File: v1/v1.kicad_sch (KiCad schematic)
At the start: 45 parts, among them CON1 SNES-CONN, M1 LY68L6400SLIT, U1 SN74LV165APWR, U2 SN74LV165APWR, U3 SN74LV165APWR, U4 SN74LVC8T245PWR, U5 PIC12F629-I/SN, U6 AMS1117-3.3, U7 SN74LVC8T245PWR, U8 Pair of 20-pin 1.27mm pitch v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

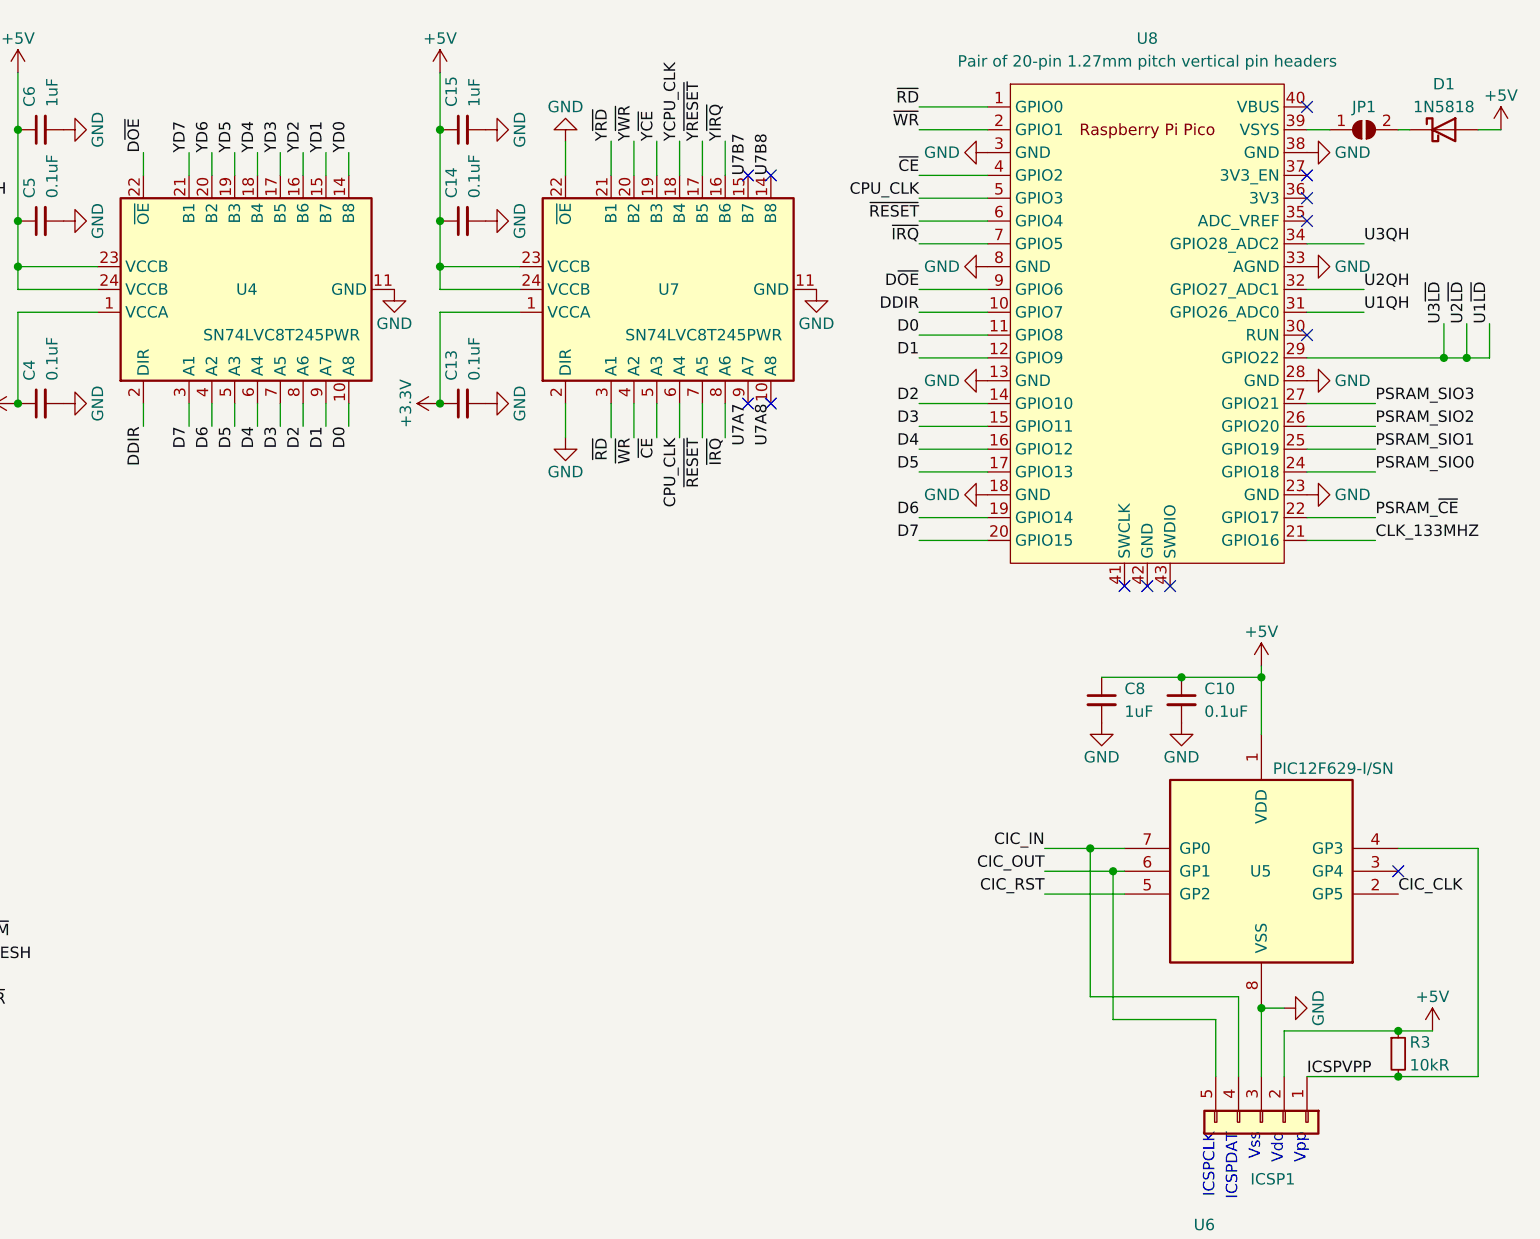
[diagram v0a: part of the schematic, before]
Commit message: v1: replace Pico component with pair of pin headers
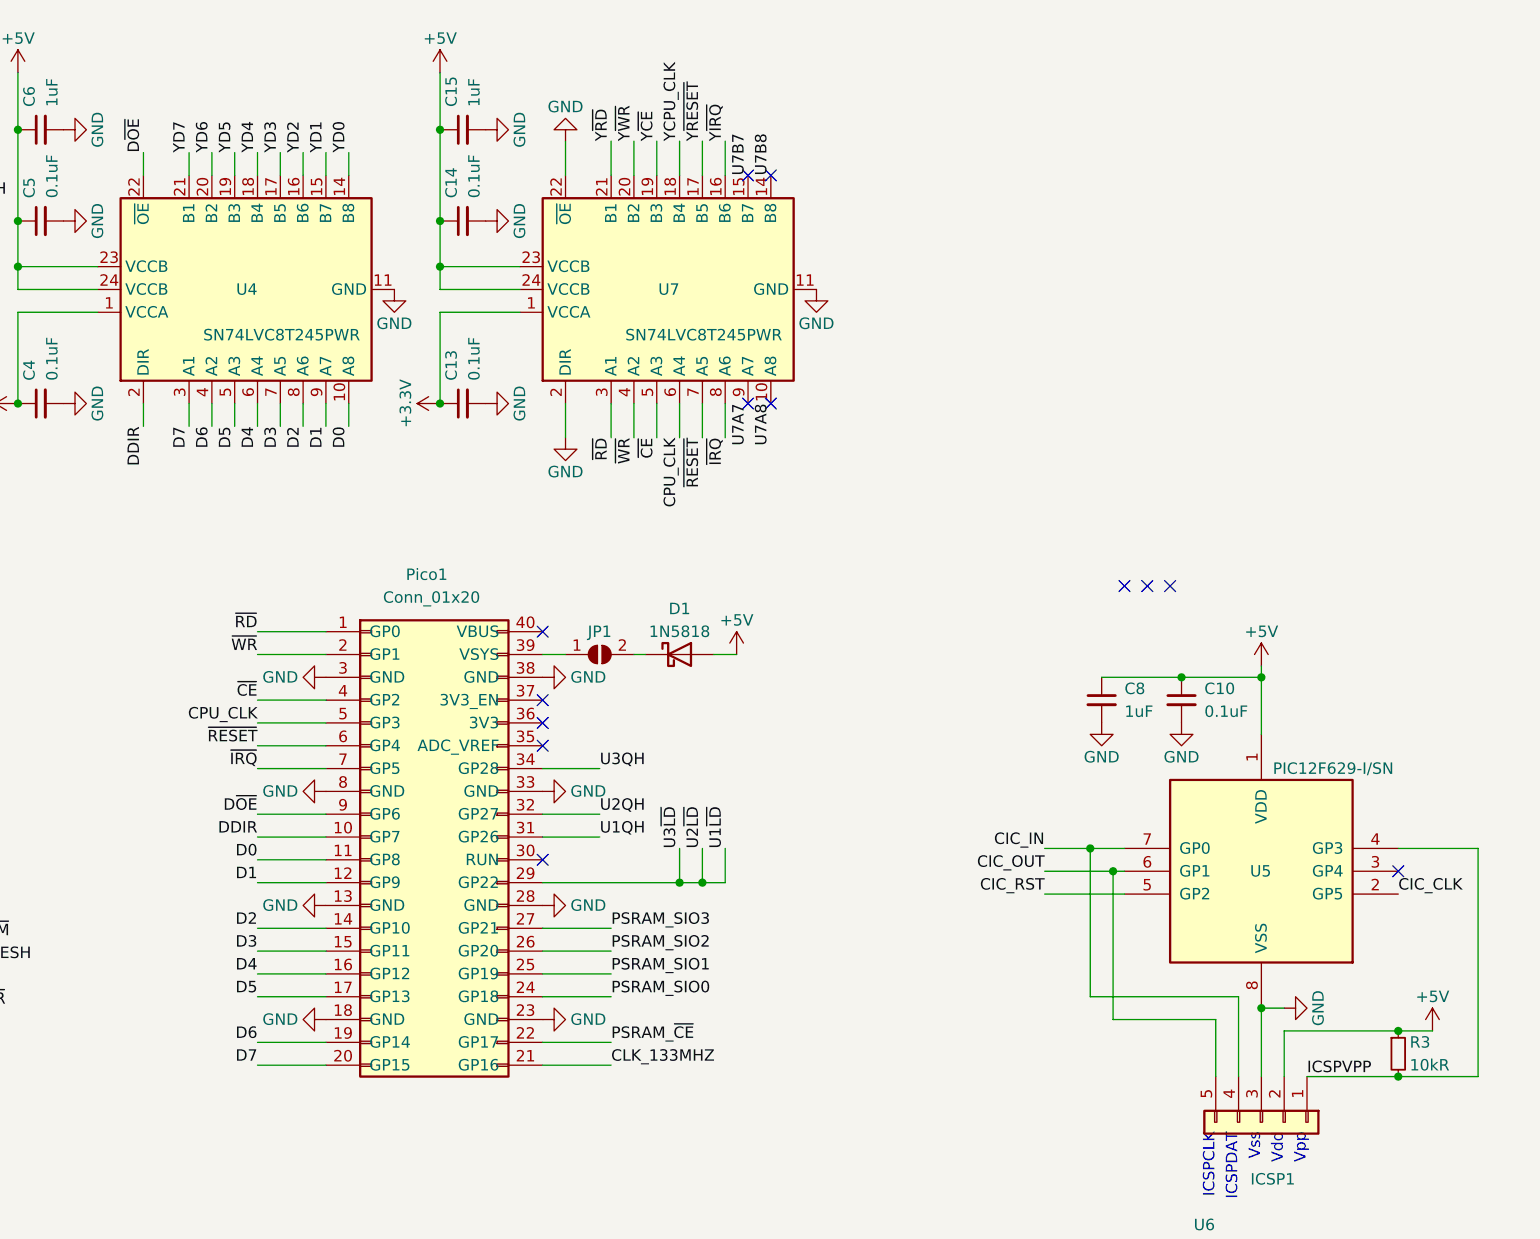
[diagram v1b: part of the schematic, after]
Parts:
- removed U8: Pair of 20-pin 1.27mm pitch vertical pin headers, RP-Pico:RPi_Pico_SMD_TH, symbol MCU_RaspberryPi_and_Boards:Pico
- added Pico1: Conn_01x20, Connector_PinHeader_2.54mm:PinHeader_1x20_P2.54mm_Vertical, symbol Connector_Generic:Conn_01x20
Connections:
- net CLK_133MHZ: now also Pico1.21 (GP16)
- net CPU_CLK: now also Pico1.5 (GP3)
- net D0: now also Pico1.11 (GP8)
- net D1: now also Pico1.12 (GP9)
- net D2: now also Pico1.14 (GP10)
- net D3: now also Pico1.15 (GP11)
- net D4: now also Pico1.16 (GP12)
- net D5: now also Pico1.17 (GP13)
- net D6: now also Pico1.19 (GP14)
- net D7: now also Pico1.20 (GP15)
- net DDIR: now also Pico1.10 (GP7)
- net D~{OE}: now also Pico1.9 (GP6)
- net GND: now also Pico1.13 (GND), Pico1.18 (GND), Pico1.23 (GND), Pico1.28 (GND), Pico1.3 (GND), Pico1.33 (GND), Pico1.38 (GND), Pico1.8 (GND)
- net PSRAM_SIO0: now also Pico1.24 (GP18)
- net PSRAM_SIO1: now also Pico1.25 (GP19)
- net PSRAM_SIO2: now also Pico1.26 (GP20)
- net PSRAM_SIO3: now also Pico1.27 (GP21)
- net PSRAM_~{CE}: now also Pico1.22 (GP17)
- net U1QH: now also Pico1.31 (GP26)
- net U1~{LD}: now also Pico1.29 (GP22)
- net U2QH: now also Pico1.32 (GP27)
- net U3QH: now also Pico1.34 (GP28)
- net ~{CE}: now also Pico1.4 (GP2)
- net ~{IRQ}: now also Pico1.7 (GP5)
- net ~{RD}: now also Pico1.1 (GP0)
- net ~{RESET}: now also Pico1.6 (GP4)
- net ~{WR}: now also Pico1.2 (GP1)
- net at JP1.1 (A): now also Pico1.39 (VSYS)

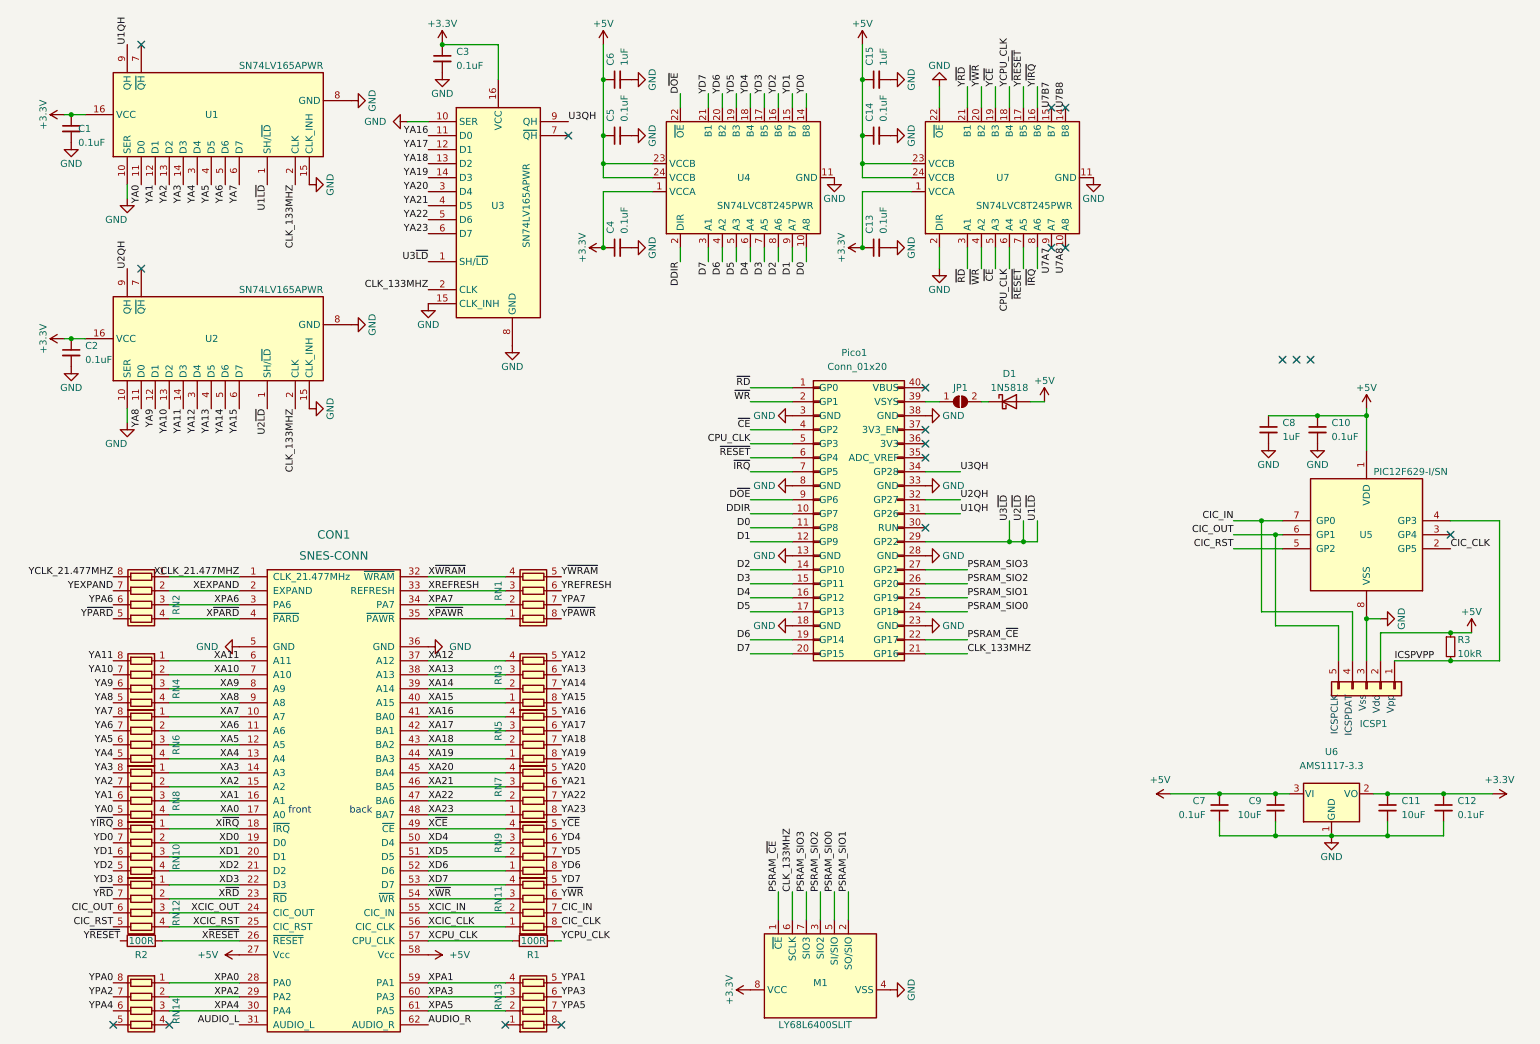
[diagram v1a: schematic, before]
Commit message: v1: redo shift regs; redo gpio pin assignments; add jumpers for LDO vs Pico 3V3 power supply; use TXS0101 for /RESET
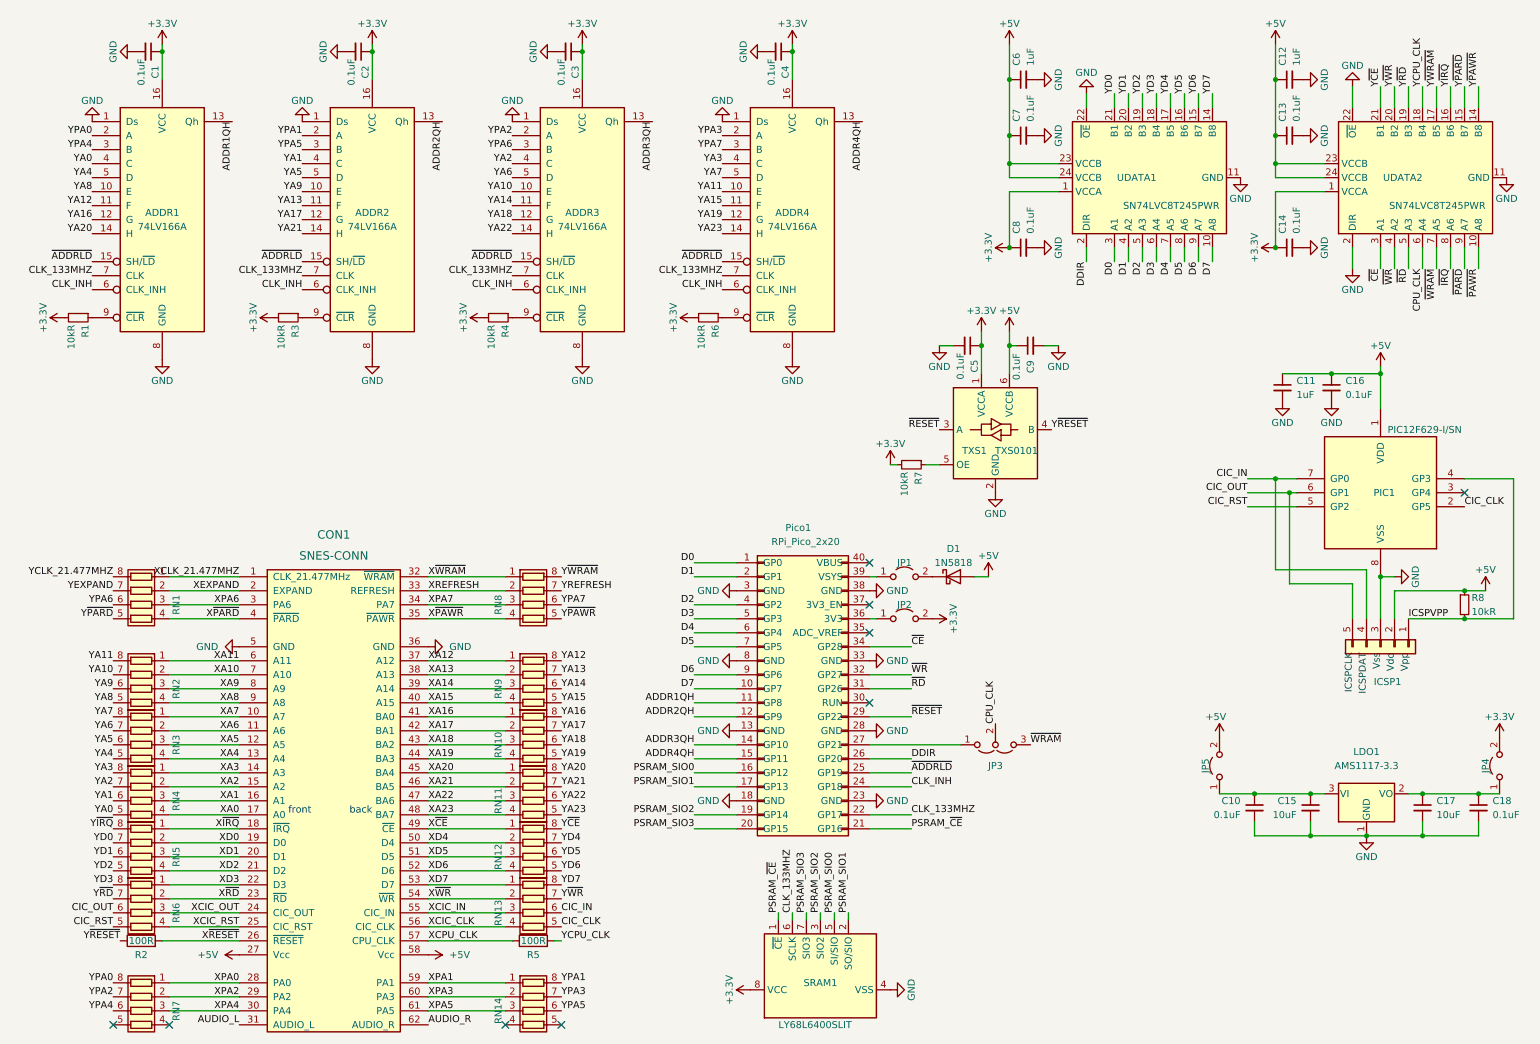
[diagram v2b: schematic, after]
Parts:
- removed RN3, RN5, RN7: 100R, Resistor_SMD:R_Array_Concave_4x0603, symbol Device:R_Pack04
- removed U1, U2, U3: SN74LV165APWR, Package_SO:TSSOP-16_4.4x5mm_P0.65mm, symbol 74xx:74HC165
- added ADDR1, ADDR2, ADDR3, ADDR4: 74LV166A, Package_SO:SOIC-16_3.9x9.9mm_P1.27mm, symbol 74xx:74LV166A
- added C4, C5, C9: 0.1uF, Capacitor_SMD:C_1206_3216Metric_Pad1.33x1.80mm_HandSolder, symbol Device:C_Small
- added JP2: PICO_3V3_EN, Connector_PinHeader_2.54mm:PinHeader_1x02_P2.54mm_Vertical, symbol Jumper:Jumper_2_Open
- added JP3: CLK_OR_WRAM, Connector_PinHeader_2.54mm:PinHeader_1x03_P2.54mm_Vertical, symbol Jumper:Jumper_3_Open
- added JP4: SNES_3V3_EN, Connector_PinHeader_2.54mm:PinHeader_1x02_P2.54mm_Vertical, symbol Jumper:Jumper_2_Open
- added JP5: LDO_EN, Connector_PinHeader_2.54mm:PinHeader_1x02_P2.54mm_Vertical, symbol Jumper:Jumper_2_Open
- added R1, R3, R4, R6, R7: 10kR, Resistor_SMD:R_1206_3216Metric_Pad1.30x1.75mm_HandSolder, symbol Device:R_Small
- added RN10, RN12, RN14: 100R, Resistor_SMD:R_Array_Concave_4x0603, symbol Device:R_Pack04
- added TXS1: TXS0101, Package_TO_SOT_SMD:SOT-23-6_Handsoldering, symbol Logic_LevelTranslator:TXS0101
- CON1: footprint sd2snes:SNESCART_EXT2_SMTUSB -> SNES:SNESCART_EXT2
- ICSP1: value Conn_01x05 -> PIC12_ICSP
- JP1: value SolderJumper_2_Open -> SNES 5V -> Pico; footprint Jumper:SolderJumper-2_P1.3mm_Open_RoundedPad1.0x1.5mm -> Connector_PinHeader_2.54mm:PinHeader_1x02_P2.54mm_Vertical; symbol Jumper:SolderJumper_2_Open -> Jumper:Jumper_2_Open
- Pico1: value Conn_01x20 -> RPi_Pico_2x20; footprint Connector_PinHeader_2.54mm:PinHeader_1x20_P2.54mm_Vertical -> RPi_Pico:RPi_Pico_2x20; symbol Connector_Generic:Conn_01x20 -> RPi_Pico:RPi_Pico
- renumbered C7 to C10, C8 to C11, C15 to C12, C14 to C13, C13 to C14, C9 to C15, C10 to C16, C11 to C17, C12 to C18, C5 to C7, C4 to C8, U6 to LDO1, U5 to PIC1, R1 to R5, R3 to R8, RN2 to RN1, RN4 to RN2, RN6 to RN3, RN8 to RN4, RN10 to RN5, RN12 to RN6, RN14 to RN7, RN1 to RN8, M1 to SRAM1, U4 to UDATA1, U7 to UDATA2
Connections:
- net U1QH is gone; now on net ~{RD}: Pico1.31 (GP26)
- net U1~{LD} is gone; now on net ~{RESET}: Pico1.29 (GP22)
- net U2QH is gone; now on net ~{WR}: Pico1.32 (GP27)
- net U3QH is gone; now on net ~{CE}: Pico1.34 (GP28)
- net U7B7 is gone; now on net Y~{PARD}: UDATA2.15 (B7)
- net U7B8 is gone; now on net Y~{PAWR}: UDATA2.14 (B8)
- net +3.3V: now also ADDR1.16 (VCC), ADDR2.16 (VCC), ADDR3.16 (VCC), ADDR4.16 (VCC), C4.1, C5.1, JP2.2 (B), JP4.2 (B), R1.2, R3.2, R4.2, R6.2, R7.2, TXS1.1 (VCCA); no longer C17.1, C18.1, LDO1.2 (VO)
- net +5V: now also C9.1, JP5.2 (B), TXS1.6 (VCCB); no longer C10.1, C15.1, LDO1.3 (VI)
- net CIC_CLK: now also RN13.5 (R4.2); no longer RN11.8 (R1.2)
- net CIC_IN: now also RN13.6 (R3.2); no longer RN11.7 (R2.2)
- net CLK_133MHZ: now also Pico1.22 (GP17), ADDR1.7 (CLK), ADDR2.7 (CLK), ADDR3.7 (CLK), ADDR4.7 (CLK); no longer Pico1.21 (GP16)
- net CPU_CLK: now also JP3.2 (C); no longer Pico1.5 (GP3)
- net D0: now also Pico1.1 (GP0), UDATA1.3 (A1); no longer Pico1.11 (GP8), UDATA1.10 (A8)
- net D1: now also Pico1.2 (GP1), UDATA1.4 (A2); no longer Pico1.12 (GP9), UDATA1.9 (A7)
- net D2: now also Pico1.4 (GP2), UDATA1.5 (A3); no longer Pico1.14 (GP10), UDATA1.8 (A6)
- net D3: now also Pico1.5 (GP3), UDATA1.6 (A4); no longer Pico1.15 (GP11), UDATA1.7 (A5)
- net D4: now also Pico1.6 (GP4), UDATA1.7 (A5); no longer Pico1.16 (GP12), UDATA1.6 (A4)
- net D5: now also Pico1.7 (GP5), UDATA1.8 (A6); no longer Pico1.17 (GP13), UDATA1.5 (A3)
- net D6: now also Pico1.9 (GP6), UDATA1.9 (A7); no longer Pico1.19 (GP14), UDATA1.4 (A2)
- net D7: now also Pico1.10 (GP7), UDATA1.10 (A8); no longer Pico1.20 (GP15), UDATA1.3 (A1)
- net DDIR: now also Pico1.26 (GP20); no longer Pico1.10 (GP7)
- net GND: now also UDATA1.22 (~{OE}), ADDR1.1 (Ds), ADDR1.8 (GND), ADDR2.1 (Ds), ADDR2.8 (GND), ADDR3.1 (Ds), ADDR3.8 (GND), ADDR4.1 (Ds), ADDR4.8 (GND), C4.2, C5.2, C9.2, TXS1.2 (GND)
- net PSRAM_SIO0: now also Pico1.16 (GP12); no longer Pico1.24 (GP18)
- net PSRAM_SIO1: now also Pico1.17 (GP13); no longer Pico1.25 (GP19)
- net PSRAM_SIO2: now also Pico1.19 (GP14); no longer Pico1.26 (GP20)
- net PSRAM_SIO3: now also Pico1.20 (GP15); no longer Pico1.27 (GP21)
- net PSRAM_~{CE}: now also Pico1.21 (GP16); no longer Pico1.22 (GP17)
- net XA12: now also RN9.1 (R1.1)
- net XA13: now also RN9.2 (R2.1)
- net XA14: now also RN9.3 (R3.1)
- net XA15: now also RN9.4 (R4.1)
- net XA16: now also RN10.1 (R1.1)
- net XA17: now also RN10.2 (R2.1)
- net XA18: now also RN10.3 (R3.1)
- net XA19: now also RN10.4 (R4.1)
- net XA20: now also RN11.1 (R1.1)
- net XA21: now also RN11.2 (R2.1)
- net XA22: now also RN11.3 (R3.1)
- net XA23: now also RN11.4 (R4.1)
- net XCIC_CLK: now also RN13.4 (R4.1); no longer RN11.1 (R1.1)
- net XCIC_IN: now also RN13.3 (R3.1); no longer RN11.2 (R2.1)
- net XD4: now also RN12.2 (R2.1); no longer RN9.3 (R3.1)
- net XD5: now also RN12.3 (R3.1); no longer RN9.2 (R2.1)
- net XD6: now also RN12.4 (R4.1); no longer RN9.1 (R1.1)
- net XD7: now also RN13.1 (R1.1); no longer RN11.4 (R4.1)
- net XPA1: now also RN14.1 (R1.1); no longer RN13.4 (R4.1)
- net XPA3: now also RN14.2 (R2.1); no longer RN13.3 (R3.1)
- net XPA5: now also RN14.3 (R3.1); no longer RN13.2 (R2.1)
- net XPA7: now also RN8.3 (R3.1); no longer RN8.2 (R2.1)
- net XREFRESH: now also RN8.2 (R2.1); no longer RN8.3 (R3.1)
- net X~{CE}: now also RN12.1 (R1.1); no longer RN9.4 (R4.1)
- net X~{PAWR}: now also RN8.4 (R4.1); no longer RN8.1 (R1.1)
- net X~{WRAM}: now also RN8.1 (R1.1); no longer RN8.4 (R4.1)
- net X~{WR}: now also RN13.2 (R2.1); no longer RN11.3 (R3.1)
- net YA0: now also ADDR1.4 (C)
- net YA1: now also ADDR2.4 (C)
- net YA10: now also ADDR3.10 (E)
- net YA11: now also ADDR4.10 (E)
- net YA12: now also RN9.8 (R1.2), ADDR1.11 (F)
- net YA13: now also RN9.7 (R2.2), ADDR2.11 (F)
- net YA14: now also RN9.6 (R3.2), ADDR3.11 (F)
- net YA15: now also RN9.5 (R4.2), ADDR4.11 (F)
- net YA16: now also ADDR1.12 (G), RN10.8 (R1.2)
- net YA17: now also ADDR2.12 (G), RN10.7 (R2.2)
- net YA18: now also ADDR3.12 (G), RN10.6 (R3.2)
- net YA19: now also ADDR4.12 (G), RN10.5 (R4.2)
- net YA2: now also ADDR3.4 (C)
- net YA20: now also RN11.8 (R1.2), ADDR1.14 (H)
- net YA21: now also RN11.7 (R2.2), ADDR2.14 (H)
- net YA22: now also RN11.6 (R3.2), ADDR3.14 (H)
- net YA23: now also RN11.5 (R4.2), ADDR4.14 (H)
- net YA3: now also ADDR4.4 (C)
- net YA4: now also ADDR1.5 (D)
- net YA5: now also ADDR2.5 (D)
- net YA6: now also ADDR3.5 (D)
- net YA7: now also ADDR4.5 (D)
- net YA8: now also ADDR1.10 (E)
- net YA9: now also ADDR2.10 (E)
- net YD0: now also UDATA1.21 (B1); no longer UDATA1.14 (B8)
- net YD1: now also UDATA1.20 (B2); no longer UDATA1.15 (B7)
- net YD2: now also UDATA1.19 (B3); no longer UDATA1.16 (B6)
- net YD3: now also UDATA1.18 (B4); no longer UDATA1.17 (B5)
- net YD4: now also UDATA1.17 (B5), RN12.7 (R2.2); no longer RN9.6 (R3.2), UDATA1.18 (B4)
- net YD5: now also UDATA1.16 (B6), RN12.6 (R3.2); no longer RN9.7 (R2.2), UDATA1.19 (B3)
- net YD6: now also UDATA1.15 (B7), RN12.5 (R4.2); no longer RN9.8 (R1.2), UDATA1.20 (B2)
- net YD7: now also RN13.8 (R1.2), UDATA1.14 (B8); no longer RN11.5 (R4.2), UDATA1.21 (B1)
- net YPA0: now also ADDR1.2 (A)
- net YPA1: now also ADDR2.2 (A), RN14.8 (R1.2); no longer RN13.5 (R4.2)
- net YPA2: now also ADDR3.2 (A)
- net YPA3: now also ADDR4.2 (A), RN14.7 (R2.2); no longer RN13.6 (R3.2)
- net YPA4: now also ADDR1.3 (B)
- net YPA5: now also ADDR2.3 (B), RN14.6 (R3.2); no longer RN13.7 (R2.2)
- net YPA6: now also ADDR3.3 (B)
- net YPA7: now also RN8.6 (R3.2), ADDR4.3 (B); no longer RN8.7 (R2.2)
- net YREFRESH: now also RN8.7 (R2.2); no longer RN8.6 (R3.2)
- net Y~{CE}: now also UDATA2.21 (B1), RN12.8 (R1.2); no longer RN9.5 (R4.2), UDATA2.19 (B3)
- net Y~{PAWR}: now also RN8.5 (R4.2); no longer RN8.8 (R1.2)
- net Y~{RD}: now also UDATA2.19 (B3); no longer UDATA2.21 (B1)
- net Y~{RESET}: now also TXS1.4 (B); no longer UDATA2.17 (B5)
- net Y~{WRAM}: now also RN8.8 (R1.2), UDATA2.17 (B5); no longer RN8.5 (R4.2)
- net Y~{WR}: now also RN13.7 (R2.2); no longer RN11.6 (R3.2)
- net ~{CE}: now also UDATA2.3 (A1); no longer Pico1.4 (GP2), UDATA2.5 (A3)
- net ~{IRQ}: no longer Pico1.7 (GP5)
- net ~{RD}: now also UDATA2.5 (A3); no longer Pico1.1 (GP0), UDATA2.3 (A1)
- net ~{RESET}: now also TXS1.3 (A); no longer Pico1.6 (GP4), UDATA2.7 (A5)
- net ~{WR}: no longer Pico1.2 (GP1)
- net at Pico1.36 (3V3): now also JP2.1 (A)
- removed net D~{OE}: Pico1.9 (GP6), UDATA1.22 (~{OE})
- net U7A7 renamed ~{PARD}
- net U7A8 renamed ~{PAWR}
- new net: C17.1, C18.1, JP4.1 (A), LDO1.2 (VO)
- new net: C10.1, C15.1, JP5.1 (A), LDO1.3 (VI)
- new net: ADDR4.9 (~{CLR}), R6.1
- new net: ADDR1.9 (~{CLR}), R1.1
- new net: ADDR3.9 (~{CLR}), R4.1
- new net: JP3.1 (A), Pico1.27 (GP21)
- new net: R7.1, TXS1.5 (OE)
- new net: ADDR2.9 (~{CLR}), R3.1
- new net ADDR1QH: ADDR1.13 (Qh), Pico1.11 (GP8)
- new net ADDR2QH: ADDR2.13 (Qh), Pico1.12 (GP9)
- new net ADDR3QH: ADDR3.13 (Qh), Pico1.14 (GP10)
- new net ADDR4QH: ADDR4.13 (Qh), Pico1.15 (GP11)
- new net CLK_INH: ADDR1.6 (CLK_INH), ADDR2.6 (CLK_INH), ADDR3.6 (CLK_INH), ADDR4.6 (CLK_INH), Pico1.24 (GP18)
- new net ~{ADDRLD}: ADDR1.15 (SH/~{LD}), ADDR2.15 (SH/~{LD}), ADDR3.15 (SH/~{LD}), ADDR4.15 (SH/~{LD}), Pico1.25 (GP19)
- new net ~{WRAM}: JP3.3 (B), UDATA2.7 (A5)
- no-connect marks 20 -> 9
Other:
- moved on the sheet: C1, C10, C11, C12, C13, C14, C15, C16, C17, C18, C2, C3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
